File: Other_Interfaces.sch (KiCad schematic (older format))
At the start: 14 parts, among them J9 2908-05WB-MG

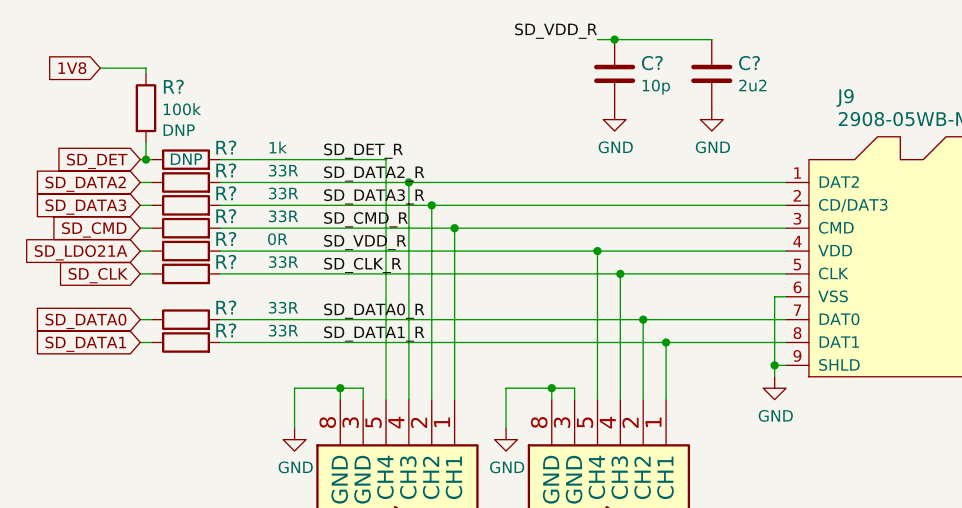
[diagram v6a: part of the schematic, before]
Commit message: Annotate parts
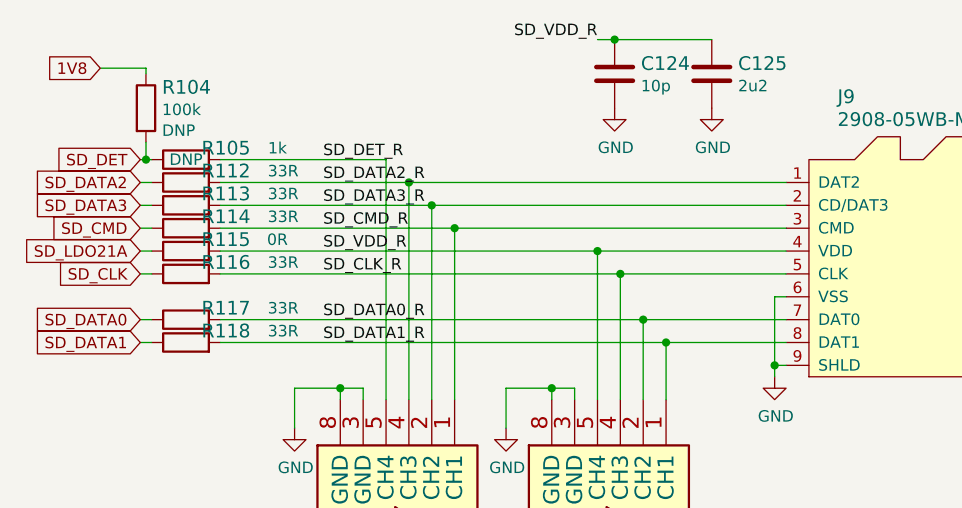
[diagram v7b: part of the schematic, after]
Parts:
- gave numbers to parts that had none: 11
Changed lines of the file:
@@
 	3425 3075 5075 3075
 $Comp
-L antmicroResistors0402:R_0R_0402 R?
+L antmicroResistors0402:R_0R_0402 R115
 U 1 1 61F42847
 P 3275 3075
-F 0 "R?" H 3450 3125 60  0000 C CNN
+F 0 "R115" H 3450 3125 60  0000 C CNN
 F 1 "R_0R_0402" H 3275 2925 60  0001 C CNN
 F 2 "antmicro-footprints:0402-res" H 3475 3275 60  0001 L CNN
@@
 SD_LDO21A
 $Comp
-L sa800u-baseboard-hw:R_1k_0402 R?
+L sa800u-baseboard-hw:R_1k_0402 R105
 U 1 1 61EB148E
 P 3275 2675
-F 0 "R?" H 3450 2725 60  0000 C CNN
+F 0 "R105" H 3450 2725 60  0000 C CNN
 F 1 "R_1k_0402" H 3275 2525 60  0001 C CNN
 F 2 "sa800u-baseboard-hw-footprints:0402-res" H 3475 2875 60  0001 L CNN
@@
 $EndComp
 $Comp
-L antmicroResistors0402:R_33R_0402 R?
+L antmicroResistors0402:R_33R_0402 R118
 U 1 1 61EAF388
 P 3275 3475
-F 0 "R?" H 3450 3525 60  0000 C CNN
+F 0 "R118" H 3450 3525 60  0000 C CNN
 F 1 "R_33R_0402" H 3275 3325 60  0001 C CNN
 F 2 "antmicro-footprints:0402-res" H 3475 3675 60  0001 L CNN
@@
 $EndComp
 $Comp
-L antmicroResistors0402:R_33R_0402 R?
+L antmicroResistors0402:R_33R_0402 R117
 U 1 1 61EAE6D0
 P 3275 3375
-F 0 "R?" H 3450 3425 60  0000 C CNN
+F 0 "R117" H 3450 3425 60  0000 C CNN
 F 1 "R_33R_0402" H 3275 3225 60  0001 C CNN
 F 2 "antmicro-footprints:0402-res" H 3475 3575 60  0001 L CNN
@@
 $EndComp
 $Comp
-L antmicroResistors0402:R_33R_0402 R?
+L antmicroResistors0402:R_33R_0402 R116
 U 1 1 61EAD860
 P 3275 3175
-F 0 "R?" H 3450 3225 60  0000 C CNN
+F 0 "R116" H 3450 3225 60  0000 C CNN
 F 1 "R_33R_0402" H 3275 3025 60  0001 C CNN
 F 2 "antmicro-footprints:0402-res" H 3475 3375 60  0001 L CNN
@@
 $EndComp
 $Comp
-L antmicroResistors0402:R_33R_0402 R?
+L antmicroResistors0402:R_33R_0402 R114
 U 1 1 61EAC664
 P 3275 2975
-F 0 "R?" H 3450 3025 60  0000 C CNN
+F 0 "R114" H 3450 3025 60  0000 C CNN
 F 1 "R_33R_0402" H 3275 2825 60  0001 C CNN
 F 2 "antmicro-footprints:0402-res" H 3475 3175 60  0001 L CNN
@@
 $EndComp
 $Comp
-L antmicroResistors0402:R_33R_0402 R?
+L antmicroResistors0402:R_33R_0402 R113
 U 1 1 61EAB8F4
 P 3275 2875
-F 0 "R?" H 3450 2925 60  0000 C CNN
+F 0 "R113" H 3450 2925 60  0000 C CNN
 F 1 "R_33R_0402" H 3275 2725 60  0001 C CNN
 F 2 "antmicro-footprints:0402-res" H 3475 3075 60  0001 L CNN
@@
 $EndComp
 $Comp
-L antmicroResistors0402:R_33R_0402 R?
+L antmicroResistors0402:R_33R_0402 R112
 U 1 1 61EAAB9C
 P 3275 2775
-F 0 "R?" H 3450 2825 60  0000 C CNN
+F 0 "R112" H 3450 2825 60  0000 C CNN
 F 1 "R_33R_0402" H 3275 2625 60  0001 C CNN
 F 2 "antmicro-footprints:0402-res" H 3475 2975 60  0001 L CNN
@@
 Connection ~ 5075 3075
 $Comp
-L sa800u-baseboard-hw:C_10p_0402 C?
+L sa800u-baseboard-hw:C_10p_0402 C124
 U 1 1 62000138
 P 5150 2300
-F 0 "C?" H 5265 2345 60  0000 L CNN
+F 0 "C124" H 5265 2345 60  0000 L CNN
 F 1 "C_10p_0402" H 5150 2150 60  0001 C CNN
 F 2 "sa800u-baseboard-hw-footprints:0402-cap" H 5350 2500 60  0001 L CNN
@@
 P 5150 2450
 AR Path="/61A60486/62009F3E" Ref="#PWR?"  Part="1"
-AR Path="/61C01D88/62009F3E" Ref="#PWR?"  Part="1"
-F 0 "#PWR?" H 5150 2200 50  0001 C CNN
+AR Path="/61C01D88/62009F3E" Ref="#PWR0184"  Part="1"
+F 0 "#PWR0184" H 5150 2200 50  0001 C CNN
 F 1 "GND" H 5155 2277 50  0000 C CNN
 F 2 "" H 5150 2450 50  0001 C CNN
@@
 P 5575 2450
 AR Path="/61A60486/6200C035" Ref="#PWR?"  Part="1"
-AR Path="/61C01D88/6200C035" Ref="#PWR?"  Part="1"
-F 0 "#PWR?" H 5575 2200 50  0001 C CNN
+AR Path="/61C01D88/6200C035" Ref="#PWR0185"  Part="1"
+F 0 "#PWR0185" H 5575 2200 50  0001 C CNN
 F 1 "GND" H 5580 2277 50  0000 C CNN
 F 2 "" H 5575 2450 50  0001 C CNN
@@
 	5150 2150 5575 2150
 $Comp
-L antmicroCapacitors0603:C_2u2_0603 C?
+L antmicroCapacitors0603:C_2u2_0603 C125
 U 1 1 62000EB0
 P 5575 2300
-F 0 "C?" H 5690 2345 60  0000 L CNN
+F 0 "C125" H 5690 2345 60  0000 L CNN
 F 1 "C_2u2_0603" H 5575 2150 60  0001 C CNN
 F 2 "antmicro-footprints:0603-cap" H 5775 2500 60  0001 L CNN
@@
 SD_VDD_R
 $Comp
-L sa800u-baseboard-hw:R_100k_0402 R?
+L sa800u-baseboard-hw:R_100k_0402 R104
 U 1 1 6202D8CA
 P 3100 2450
-F 0 "R?" V 3009 2520 60  0000 L CNN
+F 0 "R104" V 3009 2520 60  0000 L CNN
 F 1 "R_100k_0402" H 3100 2300 60  0001 C CNN
 F 2 "sa800u-baseboard-hw-footprints:0402-res" H 3300 2650 60  0001 L CNN
